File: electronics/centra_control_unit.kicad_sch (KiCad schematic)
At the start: 6 parts, among them U14 CD74HC4067SM, U15 TCA9555PWR, U18 SN74LV4051A, U4 ESP32-S3-MINI-1U

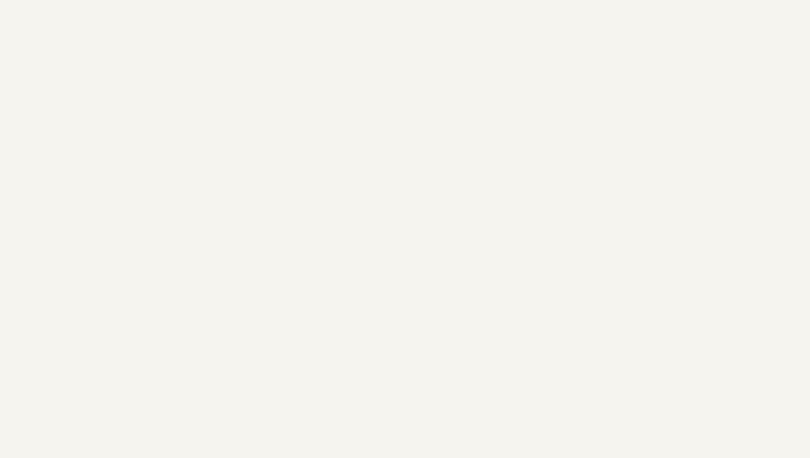
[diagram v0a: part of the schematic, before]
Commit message: basic temp sensor on RMT DS18B20. analogUI stopped working...
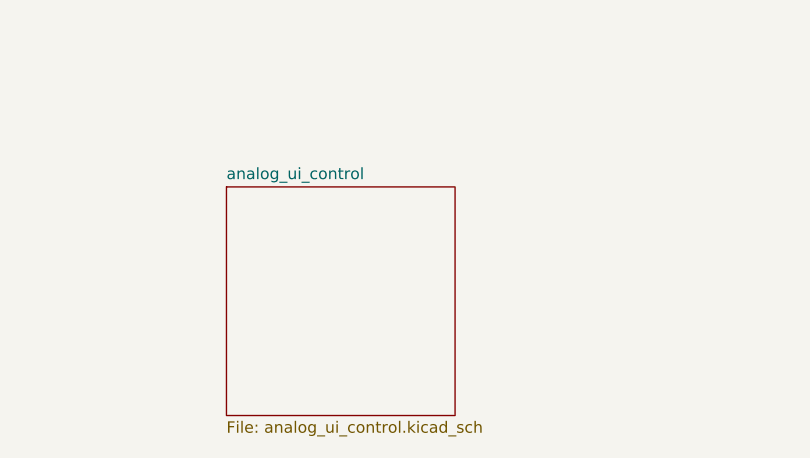
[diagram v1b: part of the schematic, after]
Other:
- added sheet analog_ui_control (analog_ui_control.kicad_sch)
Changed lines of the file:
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@@
 	(label "ch3_diag"
 		(at 226.06 119.38 0)
-		(fields_autoplaced yes)
 		(effects
 			(font
@@
 	(label "LED_B"
 		(at 146.05 63.5 0)
-		(fields_autoplaced yes)
 		(effects
 			(font
@@
 	(label "DAC_1"
 		(at 115.57 96.52 180)
-		(fields_autoplaced yes)
 		(effects
 			(font
@@
 	(label "strap pin"
 		(at 147.32 91.44 0)
-		(fields_autoplaced yes)
 		(effects
 			(font
@@
 	(label "strap pin"
 		(at 147.32 93.98 0)
-		(fields_autoplaced yes)
 		(effects
 			(font
@@
 	(label "ch4_diag"
 		(at 148.59 96.52 0)
-		(fields_autoplaced yes)
 		(effects
 			(font
@@
 	(label "SCL"
 		(at 109.22 71.12 0)
-		(fields_autoplaced yes)
 		(effects
 			(font
@@
 	(label "DAC_2"
 		(at 115.57 99.06 180)
-		(fields_autoplaced yes)
 		(effects
 			(font
@@
 	(label "ch5_diag"
 		(at 148.59 99.06 0)
-		(fields_autoplaced yes)
 		(effects
 			(font
@@
 	(label "ch2_diag"
 		(at 226.06 116.84 0)
-		(fields_autoplaced yes)
 		(effects
 			(font
@@
 	(label "SDA"
 		(at 177.8 49.53 0)
-		(fields_autoplaced yes)
 		(effects
 			(font
@@
 	(label "ch1_diag"
 		(at 148.59 83.82 0)
-		(fields_autoplaced yes)
 		(effects
 			(font
@@
 	(label "LED_B"
 		(at 27.94 163.83 0)
-		(fields_autoplaced yes)
 		(effects
 			(font
@@
 	(label "SDA"
 		(at 109.22 68.58 0)
-		(fields_autoplaced yes)
 		(effects
 			(font
@@
 	(label "ch3_diag"
 		(at 148.59 88.9 0)
-		(fields_autoplaced yes)
 		(effects
 			(font
@@
 	(label "LED_G"
 		(at 146.05 66.04 0)
-		(fields_autoplaced yes)
 		(effects
 			(font
@@
 	(label "LED_R"
 		(at 27.94 168.91 0)
-		(fields_autoplaced yes)
 		(effects
 			(font
@@
 	(label "SCL"
 		(at 177.8 52.07 0)
-		(fields_autoplaced yes)
 		(effects
 			(font
@@
 	(label "strap pin"
 		(at 115.57 53.34 180)
-		(fields_autoplaced yes)
 		(effects
 			(font
@@
 	(label "ch4_diag"
 		(at 226.06 121.92 0)
-		(fields_autoplaced yes)
 		(effects
 			(font
@@
 	(label "LED_R"
 		(at 146.05 68.58 0)
-		(fields_autoplaced yes)
 		(effects
 			(font
@@
 	(label "12V_MCU"
 		(at 49.53 21.59 0)
-		(fields_autoplaced yes)
 		(effects
 			(font
@@
 	(label "ch1_diag"
 		(at 226.06 114.3 0)
-		(fields_autoplaced yes)
 		(effects
 			(font
@@
 	(label "ch2_diag"
 		(at 148.59 86.36 0)
-		(fields_autoplaced yes)
 		(effects
 			(font
@@
 	(label "ch5_diag"
 		(at 226.06 124.46 0)
-		(fields_autoplaced yes)
 		(effects
 			(font
@@
 	(label "LED_G"
 		(at 27.94 166.37 0)
-		(fields_autoplaced yes)
 		(effects
 			(font
@@
 		(shape passive)
 		(at 107.95 68.58 180)
-		(fields_autoplaced yes)
 		(effects
 			(font
@@
 		(shape passive)
 		(at 107.95 71.12 180)
-		(fields_autoplaced yes)
 		(effects
 			(font
@@
 				)
 			)
+		)
+	)
+	(sheet
+		(at 101.6 152.4)
+		(size 25.4 25.4)
+		(fields_autoplaced yes)
+		(stroke
+			(width 0.1524)
+			(type solid)
+		)
+		(fill
+			(color 0 0 0 0.0000)
+		)
+		(property "Sheetname" "analog_ui_control"
+			(at 101.6 151.6884 0)
+			(effects
+				(font
+					(size 1.27 1.27)
+				)
+				(justify left bottom)
+			)
+		)
+		(property "Sheetfile" "analog_ui_control.kicad_sch"
+			(at 101.6 178.3846 0)
+			(effects
+				(font
+					(size 1.27 1.27)
+				)
+				(justify left top)
+			)
+		)
+		(instances
+			(project "electronics"
+				(path "/eeb1234c-eae0-4ac6-a30d-2a978d66d889/04c402f1-b99a-4823-99a0-0c7312782f29"
+					(page "16")
+				)
+			)

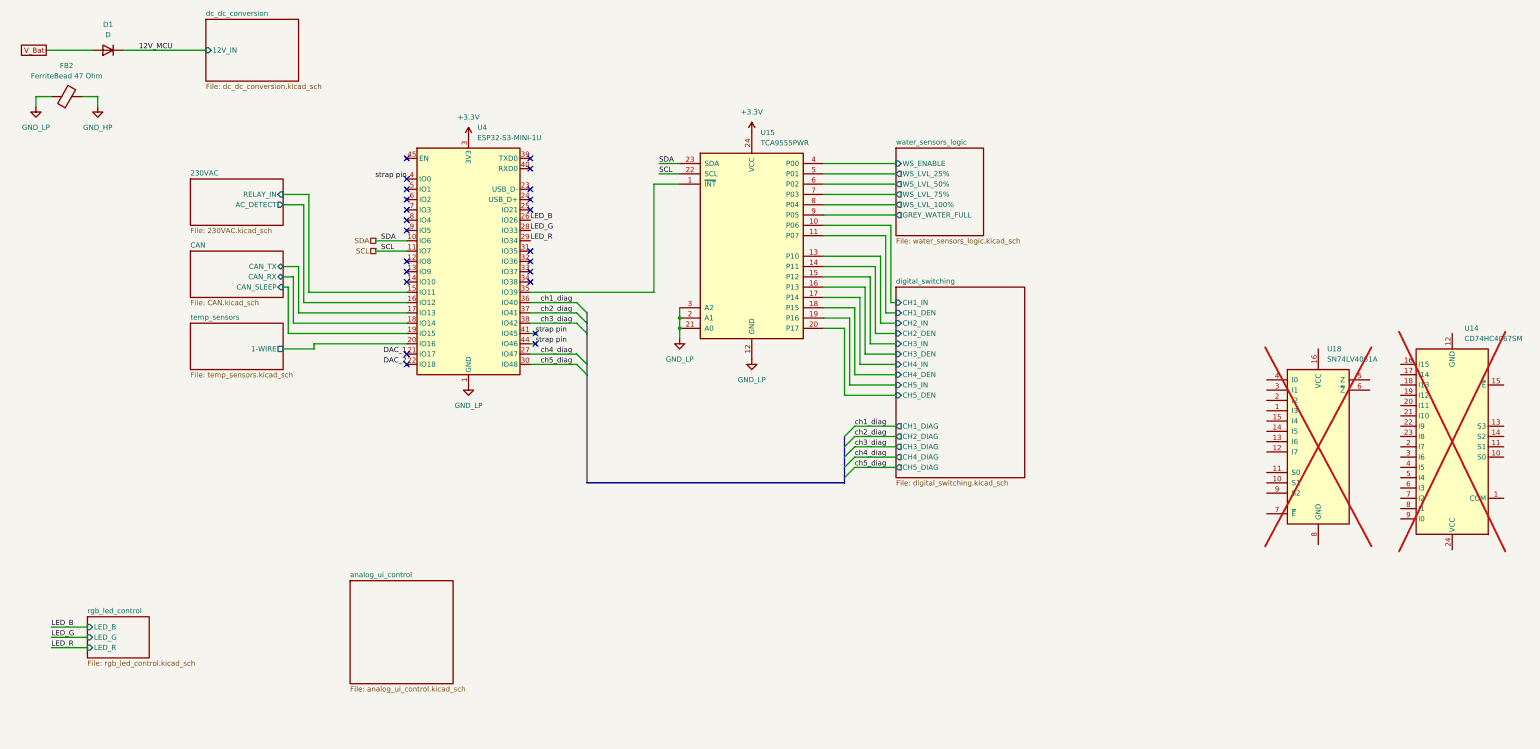
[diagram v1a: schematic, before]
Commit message: start to create BOM and finalising symbol fields
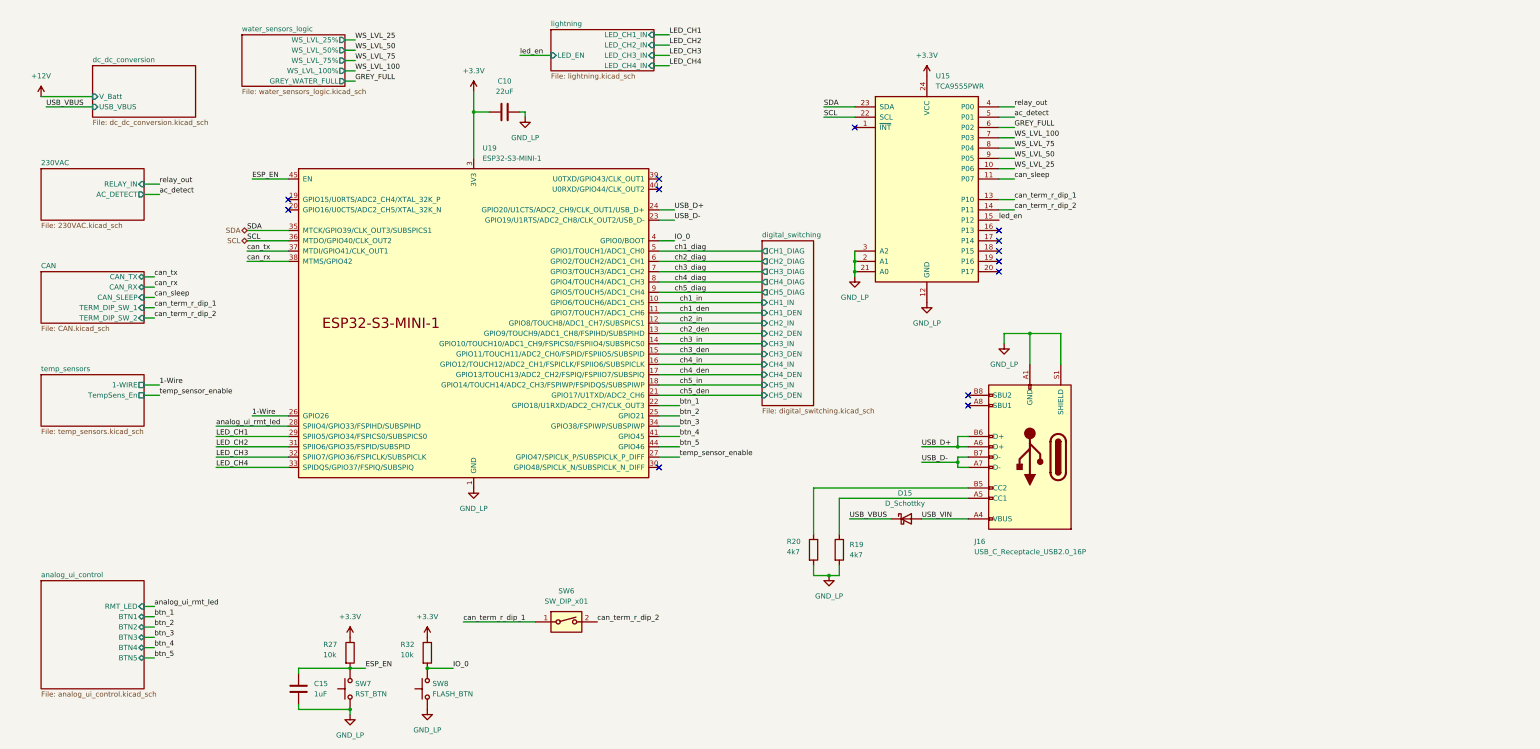
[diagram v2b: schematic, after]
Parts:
- removed D1: D, Diode_SMD:D_1210_3225Metric_Pad1.42x2.65mm_HandSolder, symbol Device:D
- removed FB2: FerriteBead 47 Ohm, Inductor_SMD:L_Walsin_WLFM201609x, symbol Device:FerriteBead
- removed U14: CD74HC4067SM, Package_SO:SSOP-24_5.3x8.2mm_P0.65mm, symbol 74xx:CD74HC4067SM
- removed U18: SN74LV4051A, symbol 74xx:74LS151
- removed U4: ESP32-S3-MINI-1U, RF_Module:ESP32-S2-MINI-1U, symbol RF_Module:ESP32-S3-MINI-1U
- added C10: 22uF, Capacitor_SMD:C_0805_2012Metric, symbol Device:C
- added C15: 1uF, Capacitor_SMD:C_0805_2012Metric, symbol Device:C
- added D15: D_Schottky, Diode_SMD:D_SMA, symbol Device:D_Schottky
- added J16: USB_C_Receptacle_USB2.0_16P, Connector_USB:USB_C_Receptacle_JAE_DX07S016JA1R1500, symbol Connector:USB_C_Receptacle_USB2.0_16P
- added R19, R20: 4k7, Resistor_SMD:R_0805_2012Metric, symbol Device:R
- added R27, R32: 10k, Resistor_SMD:R_0805_2012Metric, symbol Device:R
- added SW6: SW_DIP_x01, Connector_PinHeader_1.00mm:PinHeader_1x02_P1.00mm_Vertical, symbol Switch:SW_DIP_x01
- added SW7: RST_BTN, Button_Switch_THT:SW_PUSH_6mm_H4.3mm, symbol Switch:SW_Push
- added SW8: FLASH_BTN, Button_Switch_THT:SW_PUSH_6mm_H4.3mm, symbol Switch:SW_Push
- added U19: ESP32-S3-MINI-1, PCM_Espressif:ESP32-S3-MINI-1U, symbol PCM_Espressif:ESP32-S3-MINI-1
- U15: LCSC (none) -> C465732; TME (none) -> TCA9554APWR
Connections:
- net +3.3V: now also C10.2, R27.1, R32.1, U19.3 (3V3)
- net GND_LP: now also C10.1, C15.2, J16.A1 (GND), J16.A12 (GND), J16.B1 (GND), J16.B12 (GND), J16.S1 (SHIELD), R19.2, R20.2, SW7.1, SW8.1, U19.1 (GND), U19.2 (GND), U19.42 (GND), U19.43 (GND), U19.46 (GND), U19.47 (GND), U19.48 (GND), U19.49 (GND), U19.50 (GND), U19.51 (GND), U19.52 (GND), U19.53 (GND), U19.54 (GND), U19.55 (GND), U19.56 (GND), U19.57 (GND), U19.58 (GND), U19.59 (GND), U19.60 (GND), U19.61 (GND), U19.62 (GND), U19.63 (GND), U19.64 (GND), U19.65 (GND)
- net SCL: now also U19.36 (MTDO/GPIO40/CLK_OUT2)
- net SDA: now also U19.35 (MTCK/GPIO39/CLK_OUT3/SUBSPICS1)
- net ch1_diag: now also U19.5 (GPIO1/TOUCH1/ADC1_CH0)
- net ch2_diag: now also U19.6 (GPIO2/TOUCH2/ADC1_CH1)
- net ch3_diag: now also U19.7 (GPIO3/TOUCH3/ADC1_CH2)
- net ch4_diag: now also U19.8 (GPIO4/TOUCH4/ADC1_CH3)
- net ch5_diag: now also U19.9 (GPIO5/TOUCH5/ADC1_CH4)
- net digital_switching/CH1_DEN renamed can_sleep
- net digital_switching/CH1_IN renamed WS_LVL_25
- net digital_switching/CH2_DEN renamed can_term_r_dip_2
- net can_term_r_dip_2: now also SW6.2
- net digital_switching/CH2_IN renamed can_term_r_dip_1
- net can_term_r_dip_1: now also SW6.1
- net digital_switching/CH3_DEN: no longer names the net of U15.16 (P13)
- net digital_switching/CH3_IN renamed led_en
- net digital_switching/CH4_DEN: no longer names the net of U15.18 (P15)
- net digital_switching/CH4_IN: no longer names the net of U15.17 (P14)
- net digital_switching/CH5_DEN: no longer names the net of U15.20 (P17)
- net digital_switching/CH5_IN: no longer names the net of U15.19 (P16)
- net water_sensors_logic/GREY_WATER_FULL renamed WS_LVL_50
- net water_sensors_logic/WS_ENABLE renamed relay_out
- net water_sensors_logic/WS_LVL_100% renamed WS_LVL_75
- net water_sensors_logic/WS_LVL_25% renamed ac_detect
- net water_sensors_logic/WS_LVL_50% renamed GREY_FULL
- net water_sensors_logic/WS_LVL_75% renamed WS_LVL_100
- new net: J16.A5 (CC1), R19.1
- new net: J16.B5 (CC2), R20.1
- new net 1-Wire: U19.26 (GPIO26)
- new net ESP_EN: C15.1, R27.2, SW7.2, U19.45 (EN)
- new net IO_0: R32.2, SW8.2, U19.4 (GPIO0/BOOT)
- new net LED_CH1: U19.29 (SPIIO5/GPIO34/FSPICS0/SUBSPICS0)
- new net LED_CH2: U19.31 (SPIIO6/GPIO35/FSPID/SUBSPID)
- new net LED_CH3: U19.32 (SPIIO7/GPIO36/FSPICLK/SUBSPICLK)
- new net LED_CH4: U19.33 (SPIDQS/GPIO37/FSPIQ/SUBSPIQ)
- new net USB_D+: J16.A6 (D+), J16.B6 (D+), U19.24 (GPIO20/U1CTS/ADC2_CH9/CLK_OUT1/USB_D+)
- new net USB_D-: J16.A7 (D-), J16.B7 (D-), U19.23 (GPIO19/U1RTS/ADC2_CH8/CLK_OUT2/USB_D-)
- new net USB_VBUS: D15.1 (K)
- new net USB_VIN: D15.2 (A), J16.A4 (VBUS), J16.A9 (VBUS), J16.B4 (VBUS), J16.B9 (VBUS)
- new net analog_ui_rmt_led: U19.28 (SPIIO4/GPIO33/FSPIHD/SUBSPIHD)
- new net btn_1: U19.22 (GPIO18/U1RXD/ADC2_CH7/CLK_OUT3)
- new net btn_2: U19.25 (GPIO21)
- new net btn_3: U19.34 (GPIO38/FSPIWP/SUBSPIWP)
- new net btn_4: U19.41 (GPIO45)
- new net btn_5: U19.44 (GPIO46)
- new net can_rx: U19.38 (MTMS/GPIO42)
- new net can_tx: U19.37 (MTDI/GPIO41/CLK_OUT1)
- new net ch1_den: U19.11 (GPIO7/TOUCH7/ADC1_CH6)
- new net ch1_in: U19.10 (GPIO6/TOUCH6/ADC1_CH5)
- new net ch2_den: U19.13 (GPIO9/TOUCH9/ADC1_CH8/FSPIHD/SUBSPIHD)
- new net ch2_in: U19.12 (GPIO8/TOUCH8/ADC1_CH7/SUBSPICS1)
- new net ch3_den: U19.15 (GPIO11/TOUCH11/ADC2_CH0/FSPID/FSPIIO5/SUBSPID)
- new net ch3_in: U19.14 (GPIO10/TOUCH10/ADC1_CH9/FSPICS0/FSPIIO4/SUBSPICS0)
- new net ch4_den: U19.17 (GPIO13/TOUCH13/ADC2_CH2/FSPIQ/FSPIIO7/SUBSPIQ)
- new net ch4_in: U19.16 (GPIO12/TOUCH12/ADC2_CH1/FSPICLK/FSPIIO6/SUBSPICLK)
- new net ch5_den: U19.21 (GPIO17/U1TXD/ADC2_CH6)
- new net ch5_in: U19.18 (GPIO14/TOUCH14/ADC2_CH3/FSPIWP/FSPIDQS/SUBSPIWP)
- new net temp_sensor_enable: U19.27 (GPIO47/SPICLK_P/SUBSPICLK_P_DIFF)
- no-connect marks 23 -> 13
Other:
- removed sheet rgb_led_control
- added sheet lightning (lightning.kicad_sch)
- sheet CAN ports: added TERM_DIP_SW_1, TERM_DIP_SW_2; removed none
- sheet analog_ui_control ports: added BTN1, BTN2, BTN3, BTN4, BTN5, RMT_LED; removed none
- sheet dc_dc_conversion ports: added USB_VBUS, V_Batt; removed 12V_IN
- sheet temp_sensors ports: added TempSens_En; removed none
- sheet water_sensors_logic ports: added none; removed WS_ENABLE

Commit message: progres on layouting
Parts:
- removed J16: USB_C_Receptacle_USB2.0_16P, Connector_USB:USB_C_Receptacle_JAE_DX07S016JA1R1500, symbol Connector:USB_C_Receptacle_USB2.0_16P
- removed R19, R20: 4k7, Resistor_SMD:R_0805_2012Metric, symbol Device:R
- added J16: USB_B_Micro, Connector_USB:USB_Micro-B_Wuerth_614105150721_Vertical, symbol Connector:USB_B_Micro
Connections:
- net 1-Wire: now also U19.34 (GPIO38/FSPIWP/SUBSPIWP); no longer U19.26 (GPIO26)
- net GND_LP: now also J16.5 (GND), J16.6 (Shield)
- net LED_CH1: now also U19.33 (SPIDQS/GPIO37/FSPIQ/SUBSPIQ); no longer U19.29 (SPIIO5/GPIO34/FSPICS0/SUBSPICS0)
- net LED_CH2: now also U19.30 (GPIO48/SPICLK_N/SUBSPICLK_N_DIFF); no longer U19.31 (SPIIO6/GPIO35/FSPID/SUBSPID)
- net LED_CH3: now also U19.31 (SPIIO6/GPIO35/FSPID/SUBSPID); no longer U19.32 (SPIIO7/GPIO36/FSPICLK/SUBSPICLK)
- net LED_CH4: now also U19.32 (SPIIO7/GPIO36/FSPICLK/SUBSPICLK); no longer U19.33 (SPIDQS/GPIO37/FSPIQ/SUBSPIQ)
- net SCL: now also U19.29 (SPIIO5/GPIO34/FSPICS0/SUBSPICS0); no longer U19.36 (MTDO/GPIO40/CLK_OUT2)
- net SDA: now also U19.28 (SPIIO4/GPIO33/FSPIHD/SUBSPIHD); no longer U19.35 (MTCK/GPIO39/CLK_OUT3/SUBSPICS1)
- net USB_D+: now also J16.3 (D+)
- net USB_D-: now also J16.2 (D-)
- net USB_VIN: now also J16.1 (VBUS)
- net analog_ui_rmt_led: no longer U19.28 (SPIIO4/GPIO33/FSPIHD/SUBSPIHD)
- net btn_1: no longer U19.22 (GPIO18/U1RXD/ADC2_CH7/CLK_OUT3)
- net btn_2: now also U19.38 (MTMS/GPIO42); no longer U19.25 (GPIO21)
- net btn_3: now also U19.37 (MTDI/GPIO41/CLK_OUT1); no longer U19.34 (GPIO38/FSPIWP/SUBSPIWP)
- net btn_4: now also U19.36 (MTDO/GPIO40/CLK_OUT2); no longer U19.41 (GPIO45)
- net btn_5: now also U19.35 (MTCK/GPIO39/CLK_OUT3/SUBSPICS1); no longer U19.44 (GPIO46)
- net can_rx: now also U19.41 (GPIO45); no longer U19.38 (MTMS/GPIO42)
- net can_tx: now also U19.44 (GPIO46); no longer U19.37 (MTDI/GPIO41/CLK_OUT1)
- net ch1_den: now also U19.12 (GPIO8/TOUCH8/ADC1_CH7/SUBSPICS1); no longer U19.11 (GPIO7/TOUCH7/ADC1_CH6)
- net ch1_in: now also U19.11 (GPIO7/TOUCH7/ADC1_CH6); no longer U19.10 (GPIO6/TOUCH6/ADC1_CH5)
- net ch2_den: now also U19.10 (GPIO6/TOUCH6/ADC1_CH5); no longer U19.13 (GPIO9/TOUCH9/ADC1_CH8/FSPIHD/SUBSPIHD)
- net ch2_in: now also U19.13 (GPIO9/TOUCH9/ADC1_CH8/FSPIHD/SUBSPIHD); no longer U19.12 (GPIO8/TOUCH8/ADC1_CH7/SUBSPICS1)
- net ch3_den: now also U19.14 (GPIO10/TOUCH10/ADC1_CH9/FSPICS0/FSPIIO4/SUBSPICS0); no longer U19.15 (GPIO11/TOUCH11/ADC2_CH0/FSPID/FSPIIO5/SUBSPID)
- net ch3_in: now also U19.15 (GPIO11/TOUCH11/ADC2_CH0/FSPID/FSPIIO5/SUBSPID); no longer U19.14 (GPIO10/TOUCH10/ADC1_CH9/FSPICS0/FSPIIO4/SUBSPICS0)
- net ch4_den: now also U19.16 (GPIO12/TOUCH12/ADC2_CH1/FSPICLK/FSPIIO6/SUBSPICLK); no longer U19.17 (GPIO13/TOUCH13/ADC2_CH2/FSPIQ/FSPIIO7/SUBSPIQ)
- net ch4_in: now also U19.17 (GPIO13/TOUCH13/ADC2_CH2/FSPIQ/FSPIIO7/SUBSPIQ); no longer U19.16 (GPIO12/TOUCH12/ADC2_CH1/FSPICLK/FSPIIO6/SUBSPICLK)
- net ch5_den: now also U19.18 (GPIO14/TOUCH14/ADC2_CH3/FSPIWP/FSPIDQS/SUBSPIWP); no longer U19.21 (GPIO17/U1TXD/ADC2_CH6)
- net ch5_in: no longer U19.18 (GPIO14/TOUCH14/ADC2_CH3/FSPIWP/FSPIDQS/SUBSPIWP)
- net temp_sensor_enable: no longer U19.27 (GPIO47/SPICLK_P/SUBSPICLK_P_DIFF)
- new net digital_switching/CH5_IN: U19.21 (GPIO17/U1TXD/ADC2_CH6)
- no-connect marks 13 -> 11

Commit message: layouting progress. some 3d models upload
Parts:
- removed D15: D_Schottky, Diode_SMD:D_SMA, symbol Device:D_Schottky
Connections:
- net analog_ui_rmt_led: now also U19.40 (U0RXD/GPIO44/CLK_OUT2)
- net btn_1: now also U19.39 (U0TXD/GPIO43/CLK_OUT1)
- net can_term_r_dip_1: no longer U15.13 (P10)
- net can_term_r_dip_2: no longer U15.14 (P11)
- net temp_sensor_enable: now also U15.13 (P10)
- no-connect marks 11 -> 9
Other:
- sheet dc_dc_conversion ports: added USB_VIN; removed USB_VBUS
